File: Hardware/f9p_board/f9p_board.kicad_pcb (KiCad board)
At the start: 2 copper layers, 50 x 30 mm, 62 parts, among them J1 USB_B_Mini, J2 USB_B_Mini, J4 CAN, P1 SWD, SW1 F9P_USB_POWER, U1 Ublox_ZED_F9P, U2 STM32F405RGTx, U3 MCP16311MS, U4 ncv8705, U5 BMI160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

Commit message: adding power-supply components, rerouting needed!
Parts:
- added C27: 0.01u, Capacitor_SMD:C_0603_1608Metric, F.Cu at (45.7, 57.6)
- added C28: 2.2u, Capacitor_SMD:C_0603_1608Metric, F.Cu at (53.8, 78.2)
- added C29: 2.2u, Capacitor_SMD:C_0603_1608Metric, F.Cu at (38.2, 61.1)
- added C30: 2.2u, Capacitor_SMD:C_0603_1608Metric, F.Cu at (38.2, 57.1)
- added C31: 2.2u, Capacitor_SMD:C_0603_1608Metric, F.Cu at (40.7, 61.1)
- added C32: 4700p, Capacitor_SMD:C_0603_1608Metric, F.Cu at (44.6, 61.6)
- added C33: 0.1u, Capacitor_SMD:C_0603_1608Metric, F.Cu at (40.7, 57.1)
- added C34: 47p, Capacitor_SMD:C_0603_1608Metric, F.Cu at (38.2, 53.1)
- added C35: 47u, Capacitor_SMD:C_0603_1608Metric, F.Cu at (47.1, 61.6)
- added C36: 47u, Capacitor_SMD:C_0603_1608Metric, F.Cu at (53.8, 82.2)
- added C37: 47u, Capacitor_SMD:C_0603_1608Metric, F.Cu at (40.7, 53.1)
- added J3: BAT_CONN, TerminalBlock_Phoenix:TerminalBlock_Phoenix_PT-1,5-2-5.0-H_1x02_P5.00mm_Horizontal, F.Cu at (48.4, 72.2)
- added J5: USB_A_PWR_OUTPUT, Connector_USB:USB_A_Stewart_SS-52100-001_Horizontal, F.Cu at (33.4, 88.3)
- added L3: 7.2u, Inductor_SMD:L_10.4x10.4_H4.8, F.Cu at (36.6, 69.8)
- added R15: 243k, Resistor_SMD:R_0603_1608Metric, F.Cu at (43.2, 53.6)
- added R16: 16.9k, Resistor_SMD:R_0603_1608Metric, F.Cu at (52.1, 61.6)
- added R17: 1k, Resistor_SMD:R_0603_1608Metric, F.Cu at (48.2, 57.6)
- added R18: 49.9 Ohm, Resistor_SMD:R_0603_1608Metric, F.Cu at (45.7, 53.6)
- added R19: 53.6k, Resistor_SMD:R_0603_1608Metric, F.Cu at (43.2, 57.6)
- added R20: 10.2k, Resistor_SMD:R_0603_1608Metric, F.Cu at (49.6, 61.6)
- added SW2: MCU_USB_POWER, Button_Switch_SMD:SW_SPDT_PCM12, B.Cu at (52.8, 90.5)
- added U8: TPS54561DPRR, Package_SON:Texas_S-PWSON-N10, F.Cu at (50.0, 81.5)
- added U9: PDS760-13, POWERDI5:POWERDI5, F.Cu at (34.2, 58.3)
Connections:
- C1 pad 1: MCU_USB_VBUS -> PWR_5V
- SW1 pad 2: MCU_USB_VBUS -> PWR_5V
- U3 pad 3: MCU_USB_VBUS -> PWR_5V
- U3 pad 4: MCU_USB_VBUS -> PWR_5V
- U4 pad GND: GND -> (no net)
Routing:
- net GND: track 486.7 -> 489.5 mm, vias 79 -> 82

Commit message: updating component footprints for inductor and caps on dcdc part
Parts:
- added J6: Conn_01x02_Female, Connector_JST:JST_PH_B2B-PH-K_1x02_P2.00mm_Vertical, F.Cu at (48.7, 77.6)
- C28, C29, C30, C31: footprint Capacitor_SMD:C_0603_1608Metric -> Capacitor_SMD:C_1206_3216Metric
- L3: footprint Inductor_SMD:L_10.4x10.4_H4.8 -> Inductor_SMD:L_12x12mm_H8mm
- R17: value 1k -> 39k; footprint Resistor_SMD:R_0603_1608Metric -> Connector_JST:JST_PH_B2B-PH-K_1x02_P2.00mm_Vertical
- R18: value 49.9 Ohm -> 2.2k
- SW2: moved to F.Cu
- moved R15 34.8 mm to (31.6, 86.4), turned to 0 degrees
- moved C27 30.5 mm to (35.6, 86.4), turned to 0 degrees
- moved R18 29.8 mm to (52.1, 82.7), turned to 0 degrees
- moved C34 29.2 mm to (55.6, 76.5), turned to 0 degrees
- moved J3 29.0 mm to (21.0, 81.7), turned to 0 degrees
- moved J5 27.6 mm to (23.2, 62.7), turned to 0 degrees
- moved C37 25.7 mm to (55.6, 74.0), turned to 0 degrees
- moved C33 25.4 mm to (59.7, 74.0), turned to 0 degrees
- moved C30 24.9 mm to (62.5, 62.3), turned to 0 degrees
- moved R19 24.8 mm to (55.6, 79.0), turned to 0 degrees
- moved C32 23.9 mm to (48.1, 85.2), turned to 0 degrees
- moved C29 23.1 mm to (32.4, 83.5), turned to 0 degrees
- moved C31 22.5 mm to (38.0, 83.5), turned to 0 degrees
- moved U9 21.9 mm to (55.4, 63.4), turned to 0 degrees
- moved C28 21.5 mm to (32.4, 78.4), turned to 0 degrees
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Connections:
- R17 pad 1: VCC -> BAT_VIN
- R17 pad 2: PWR_OK -> VOLT_METER
- R18 pad 1: Net-(R18-Pad1) -> VOLT_METER
- R18 pad 2: PWR_5V -> GND
- R19 pad 2: Net-(R18-Pad1) -> PWR_5V
- U8 pad 10: PWR_OK -> Net-(U8-Pad10)

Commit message: f9p_board: Added dcdc. todo: routing
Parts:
- C1, C2, R8: moved to F.Cu
- C20, C33, R4, R5, SW2: moved to B.Cu
- R17: footprint Connector_JST:JST_PH_B2B-PH-K_1x02_P2.00mm_Vertical -> Resistor_SMD:R_0603_1608Metric
- U9: value PDS760-13 -> 3PIN_DIODE
- moved SW2 67.0 mm to (106.3, 91.7), turned to 180 degrees
- moved J5 51.6 mm to (71.1, 81.7)
- moved P1 46.9 mm to (117.6, 68.2), turned to -90 degrees
- moved J3 35.8 mm to (56.1, 89.1)
- moved R15 28.7 mm to (59.2, 78.8)
- moved C4 25.5 mm to (77.0, 66.2)
- moved L1 25.4 mm to (77.1, 70.9), turned to -90 degrees
- moved C27 25.4 mm to (59.2, 77.2)
- moved H1 24.9 mm to (49.3, 57.5)
- moved H2 24.7 mm to (49.0, 90.0)
- moved C29 23.8 mm to (55.0, 76.2), turned to 180 degrees
- moved U3 23.1 mm to (72.7, 75.8)
- moved C3 23.1 mm to (76.8, 75.8)
- moved C2 22.9 mm to (72.7, 78.5)
- moved C28 22.7 mm to (55.0, 78.6), turned to 180 degrees
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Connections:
- U2 pad 8: Net-(U2-Pad8) -> VOLT_METER
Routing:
- net GND: track 489.5 -> 75.2 mm, vias 82 -> 4
- net VCC: track 151.4 -> 0.00 mm, vias 11 -> 0
- net MCU_USB_VBUS: track 76.1 -> 0.00 mm, vias 6 -> 0
- net SWCLK: track 66.6 -> 0.00 mm, vias 4 -> 0
- net VOLT_METER: track 0.00 -> 55.5 mm, vias 0 -> 2
- net SWDIO: track 54.9 -> 0.00 mm, vias 3 -> 0
- net NRST: track 50.9 -> 0.00 mm, vias 4 -> 0
- net TIMEPULSE: track 44.2 -> 0.00 mm, vias 3 -> 0
- net F9P_RESET_N: track 43.2 -> 0.00 mm, vias 3 -> 0
- net IMU_INT2: track 32.5 -> 0.00 mm, vias 4 -> 0
- net MCU_RX_F9P_TX: track 29.0 -> 0.00 mm, vias 1 -> 0
- net SCL: track 27.6 -> 0.00 mm
- net MCU_TX_F9P_RX: track 27.0 -> 0.00 mm, vias 1 -> 0
- net SDA: track 26.7 -> 0.00 mm
- net PWR_5V: track 0.00 -> 24.2 mm
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- removed copper zone on B.Cu, net GND
- removed copper zone on F.Cu, net GND
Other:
- board size 50 x 30 mm -> 75 x 41 mm

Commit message: started routing
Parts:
- moved U8 0.20 mm to (60.1, 73.8)
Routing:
- net GND: track 75.2 -> 139.9 mm, vias 4 -> 9
- net SW: track 0.00 -> 25.6 mm, vias 0 -> 2
- net PWR_5V: track 24.2 -> 40.8 mm
- net Net-(R1-Pad1): track 0.00 -> 11.9 mm, vias 0 -> 2
- net Net-(J6-Pad2): track 0.00 -> 11.7 mm, vias 0 -> 1
- net FB: track 0.00 -> 11.0 mm, vias 0 -> 2
- net BAT_VIN: track 21.6 -> 26.7 mm
- net Net-(R15-Pad1): track 0.00 -> 4.78 mm
- net Net-(C32-Pad1): track 0.00 -> 4.52 mm
- net Net-(C27-Pad1): track 0.00 -> 3.97 mm
- net Net-(C34-Pad1): track 0.00 -> 3.60 mm
- net Net-(C33-Pad1): track 0.00 -> 2.81 mm, vias 0 -> 1
- added copper zone on F.Cu, net BAT_VIN

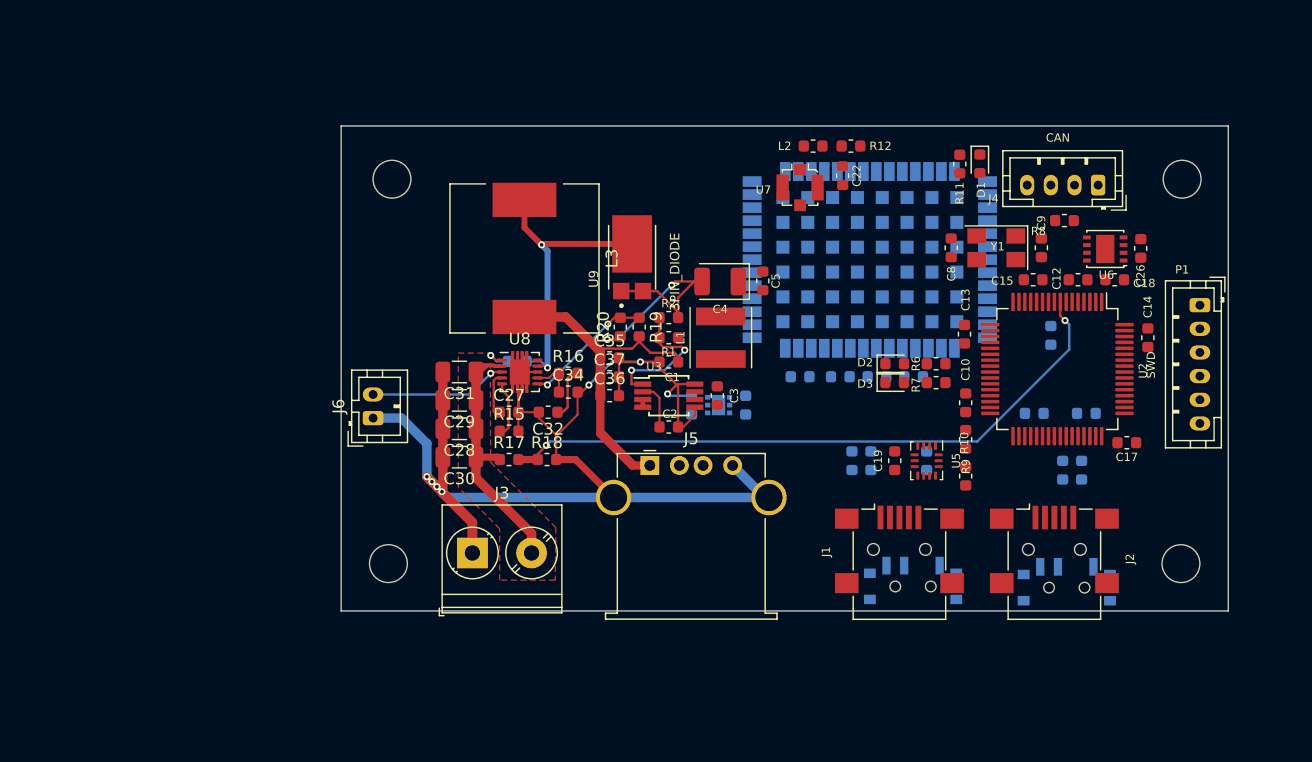
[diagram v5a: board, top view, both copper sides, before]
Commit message: f9p_board : started routing with redesign of dcdc powersupply
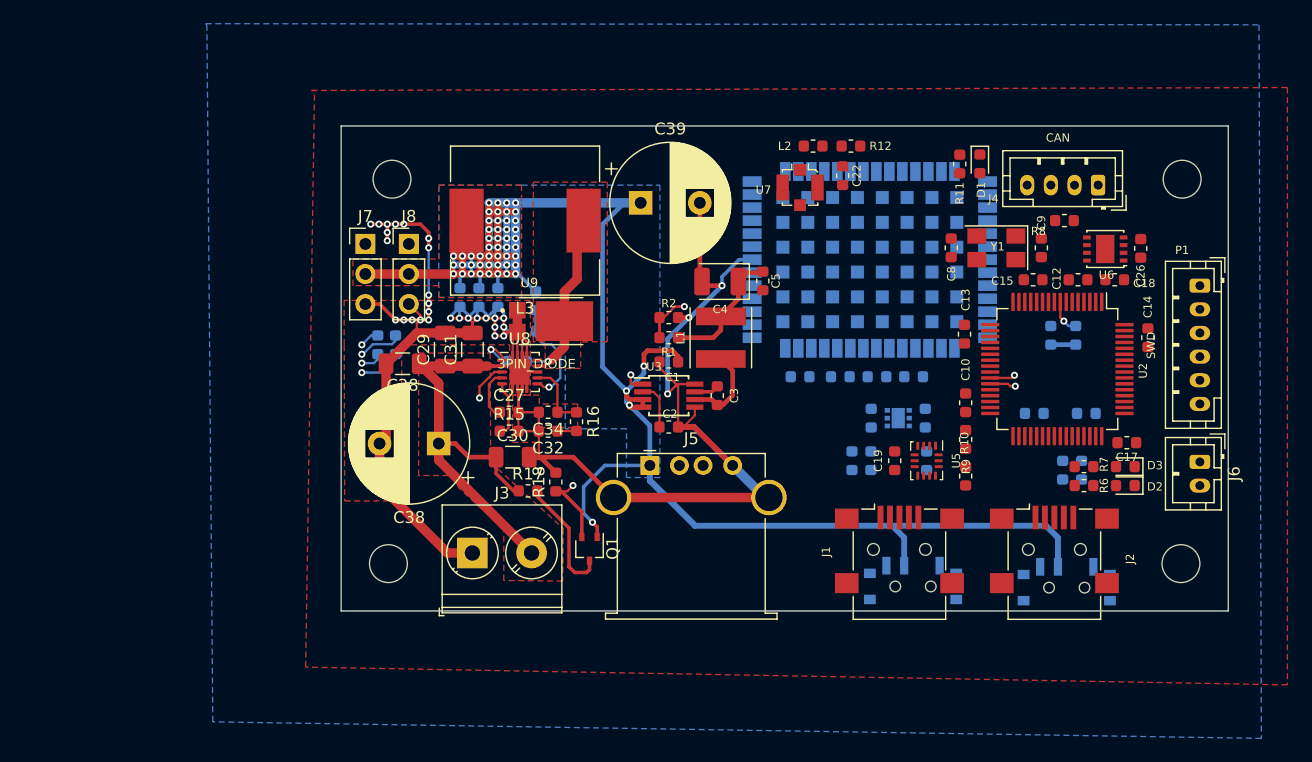
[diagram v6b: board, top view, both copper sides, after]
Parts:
- added C38: 100u, Capacitor_THT:CP_Radial_D10.0mm_P5.00mm, F.Cu at (53.2, 79.8)
- added C39: 470u, Capacitor_THT:CP_Radial_D10.0mm_P5.00mm, F.Cu at (70.3, 59.5)
- added C40: 0.1u, Capacitor_SMD:C_0603_1608Metric, B.Cu at (107.1, 70.7)
- added J7: SERV_0, Connector_PinHeader_2.54mm:PinHeader_1x03_P2.54mm_Vertical, F.Cu at (47.0, 63.0)
- added J8: SERV_1, Connector_PinHeader_2.54mm:PinHeader_1x03_P2.54mm_Vertical, F.Cu at (50.7, 63.0)
- added Q1: DMN62D0UW-7, Package_TO_SOT_SMD:SOT-323_SC-70, F.Cu at (66.0, 88.8)
- added R21: 220R, Resistor_SMD:R_0603_1608Metric, B.Cu at (48.1, 71.5)
- added R22: 220R, Resistor_SMD:R_0603_1608Metric, B.Cu at (49.6, 71.5)
- C35, C36, C37: value 47u -> 2.2u; moved to B.Cu
- J6: value Conn_01x02_Female -> EN_BAT_VIN
- R19, R20: moved to B.Cu
- moved J6 70.0 mm to (117.6, 81.4), turned to -90 degrees
- moved D2 22.1 mm to (111.3, 83.4), turned to 180 degrees
- moved D3 20.8 mm to (111.3, 81.8), turned to 180 degrees
- moved R6 16.2 mm to (107.8, 83.4), turned to 180 degrees
- moved C6 15.2 mm to (89.8, 77.7)
- moved C7 15.2 mm to (94.4, 77.7)
- moved U4 15.2 mm to (92.1, 77.7)
- moved R7 14.4 mm to (107.8, 81.8), turned to 180 degrees
- moved C35 13.6 mm to (55.0, 67.5), turned to -90 degrees
- moved C37 12.9 mm to (56.6, 67.5), turned to -90 degrees
- moved C36 12.6 mm to (58.2, 67.5), turned to -90 degrees
- moved R19 9.03 mm to (61.5, 67.8), turned to 90 degrees
- moved U9 8.72 mm to (62.8, 69.5), turned to 0 degrees
- moved R20 7.91 mm to (60.7, 70.3), turned to 0 degrees
- moved C28 7.30 mm to (50.2, 73.1)
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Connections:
- C7 pad 1: MCU_USB_VBUS -> F9P_USB_VBUS
- R17 pad 2: VOLT_METER -> Net-(Q1-Pad3)
- R6 pad 2: Net-(R6-Pad2) -> LED0
- R7 pad 2: Net-(R7-Pad2) -> LED1
- U2 pad 26: Net-(R6-Pad2) -> Net-(R21-Pad2)
- U2 pad 27: Net-(R7-Pad2) -> Net-(R22-Pad2)
- U2 pad 28: Net-(U2-Pad28) -> LED0
- U2 pad 55: Net-(U2-Pad55) -> LED1
- U4 pad 4: MCU_USB_VBUS -> F9P_USB_VBUS
- U4 pad 6: MCU_USB_VBUS -> F9P_USB_VBUS
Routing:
- net PWR_5V: track 40.8 -> 255.3 mm, vias 0 -> 52
- net Net-(R22-Pad2): track 0.00 -> 62.0 mm, vias 0 -> 2
- net Net-(R21-Pad2): track 0.00 -> 60.3 mm, vias 0 -> 2
- net Net-(J6-Pad2): track 11.7 -> 67.4 mm
- net GND: track 139.9 -> 176.0 mm, vias 9 -> 31
- net Net-(J8-Pad1): track 0.00 -> 15.6 mm, vias 0 -> 1
- net Net-(J7-Pad1): track 0.00 -> 12.4 mm, vias 0 -> 1
- net BAT_VIN: track 26.7 -> 38.3 mm
- net VCC: track 0.00 -> 11.0 mm
- net Net-(Q1-Pad3): track 0.00 -> 10.3 mm
- net SW: track 25.6 -> 17.1 mm, vias 2 -> 1
- net Net-(C3-Pad2): track 0.00 -> 7.21 mm
- net VOLT_METER: track 55.5 -> 58.8 mm
- net Net-(R1-Pad1): track 11.9 -> 15.1 mm
- net Net-(C32-Pad1): track 4.52 -> 1.62 mm
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- added copper zone on B.Cu, net GND
- added copper zone on F.Cu, net GND
- added copper zone on B.Cu, net PWR_5V
- added copper zone on F.Cu, net PWR_5V
- added copper zone on F.Cu, net SW
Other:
- copper layers 2 -> 4

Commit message: f9p_board: progress with routing
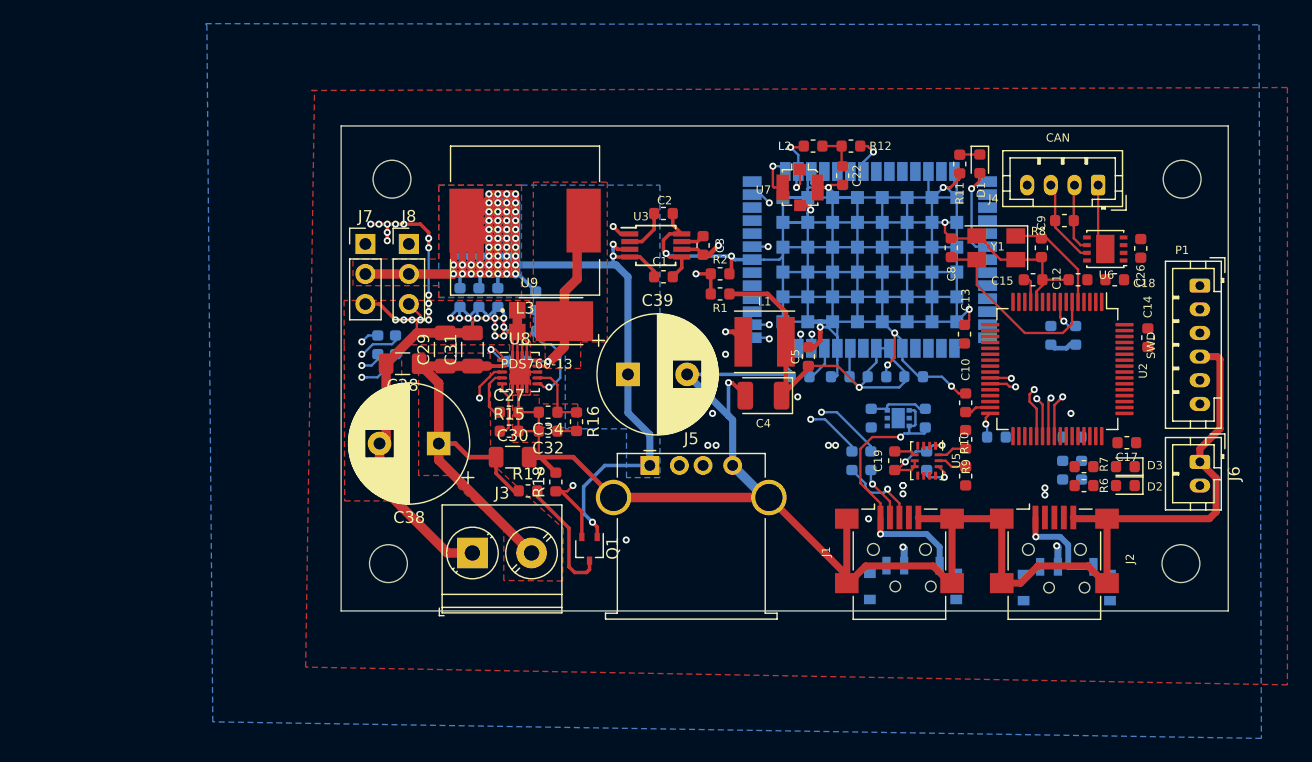
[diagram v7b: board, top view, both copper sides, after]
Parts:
- U9: value 3PIN_DIODE -> PDS760-13
- moved C2 18.1 mm to (72.2, 60.4)
- moved C39 14.5 mm to (69.2, 74.0)
- moved C3 12.8 mm to (75.6, 63.1)
- moved U3 12.7 mm to (71.6, 63.1)
- moved C4 10.3 mm to (80.7, 75.8)
- moved C5 7.47 mm to (84.5, 72.5), turned to 90 degrees
- moved C1 7.21 mm to (72.2, 65.8), turned to 0 degrees
- moved R1 5.70 mm to (77.0, 67.2)
- moved R2 5.70 mm to (77.0, 65.5)
- moved C16 3.77 mm to (100.4, 79.3)
- moved L1 3.72 mm to (80.8, 71.2), turned to 180 degrees
- moved C11 2.33 mm to (106.8, 79.3)
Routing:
- net GND: track 176.0 -> 547.5 mm, vias 31 -> 43
- net PWR_5V: track 255.3 -> 298.0 mm, vias 52 -> 62
- net TIMEPULSE: track 0.00 -> 36.9 mm, vias 0 -> 2
- net F9P_RESET_N: track 0.00 -> 36.9 mm, vias 0 -> 2
- net VCC: track 11.0 -> 46.7 mm, vias 0 -> 3
- net MCU_TX_F9P_RX: track 0.00 -> 33.1 mm, vias 0 -> 2
- net MCU_RX_F9P_TX: track 0.00 -> 33.0 mm, vias 0 -> 2
- net F9P_USB_VBUS: track 0.00 -> 24.4 mm, vias 0 -> 2
- net Net-(C8-Pad2): track 0.00 -> 16.3 mm
- net Net-(R4-Pad2): track 0.00 -> 14.1 mm, vias 0 -> 2
- net Net-(R5-Pad2): track 0.00 -> 13.9 mm, vias 0 -> 2
- net Net-(C9-Pad2): track 0.00 -> 9.17 mm
- net MCU_USB_VBUS: track 0.00 -> 8.65 mm, vias 0 -> 1
- net Net-(D1-Pad2): track 0.00 -> 7.65 mm, vias 0 -> 1
- net CANH: track 0.00 -> 7.30 mm
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- added copper zone on In1.Cu, net GND
- added copper zone on In2.Cu, net GND

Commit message: f9p_board: connecting CAN 5v to PWR_5V net. Also everything routed - first attempt
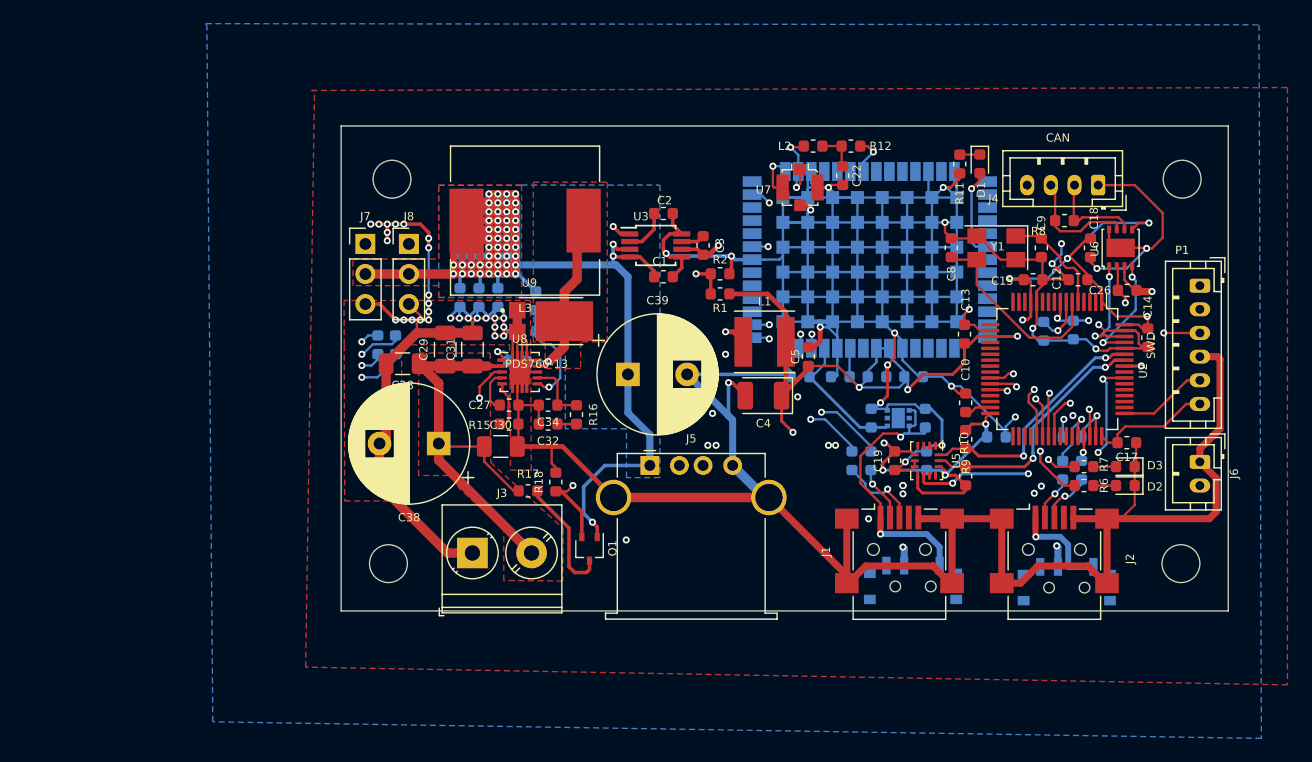
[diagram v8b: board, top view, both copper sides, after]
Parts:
- moved C26 3.73 mm to (111.5, 66.9), turned to 0 degrees
- moved C18 3.39 mm to (108.3, 63.3), turned to -90 degrees
- moved C30 1.35 mm to (58.5, 80.1)
- moved U6 1.30 mm to (110.9, 63.3), turned to 90 degrees
- moved C21 0.69 mm to (104.4, 70.3)
- moved C27 0.60 mm to (59.2, 76.6)
- moved C34 0.60 mm to (62.5, 76.6)
- moved C32 0.60 mm to (62.5, 78.2)
- moved R15 0.60 mm to (59.2, 78.2)
- moved R16 0.60 mm to (64.9, 77.4)
- moved C40 0.49 mm to (106.9, 70.2)
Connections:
- C26 pad 2: MCU_USB_VBUS -> PWR_5V
- J4 pad 4: MCU_USB_VBUS -> PWR_5V
- U6 pad 3: MCU_USB_VBUS -> PWR_5V
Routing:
- net VCC: track 46.7 -> 151.6 mm, vias 3 -> 13
- net GND: track 547.5 -> 622.0 mm, vias 43 -> 54
- net PWR_5V: track 298.0 -> 346.0 mm, vias 62 -> 63
- net IMU_INT2: track 0.00 -> 25.4 mm, vias 0 -> 3
- net SCL: track 2.50 -> 21.2 mm, vias 0 -> 2
- net SDA: track 2.50 -> 21.1 mm, vias 0 -> 2
- net NRST: track 0.00 -> 17.0 mm, vias 0 -> 1
- net LED1: track 0.00 -> 15.4 mm, vias 0 -> 3
- net SWDIO: track 0.00 -> 14.4 mm, vias 0 -> 2
- net LED0: track 0.00 -> 12.4 mm, vias 0 -> 2
- net CAN_RX: track 0.00 -> 9.56 mm, vias 0 -> 2
- net CAN_TX: track 0.00 -> 9.21 mm, vias 0 -> 2
- net F9P_3v3: track 3.09 -> 11.5 mm
- net SWCLK: track 0.00 -> 7.53 mm
- net Net-(R13-Pad2): track 0.00 -> 5.94 mm, vias 0 -> 1
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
